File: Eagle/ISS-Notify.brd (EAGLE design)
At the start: 63.5 x 63.5 mm, 68 parts, among them J1 ZX62D-B-5P8, J3 PROTOSPACE2, SW1 9077-1, U1 ATMEGA32U4, U2 MCP7940N, U3 TPS63001, U4 MCP73811, U5 TLC5971, U6 TLC5971, X1 8 MHz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

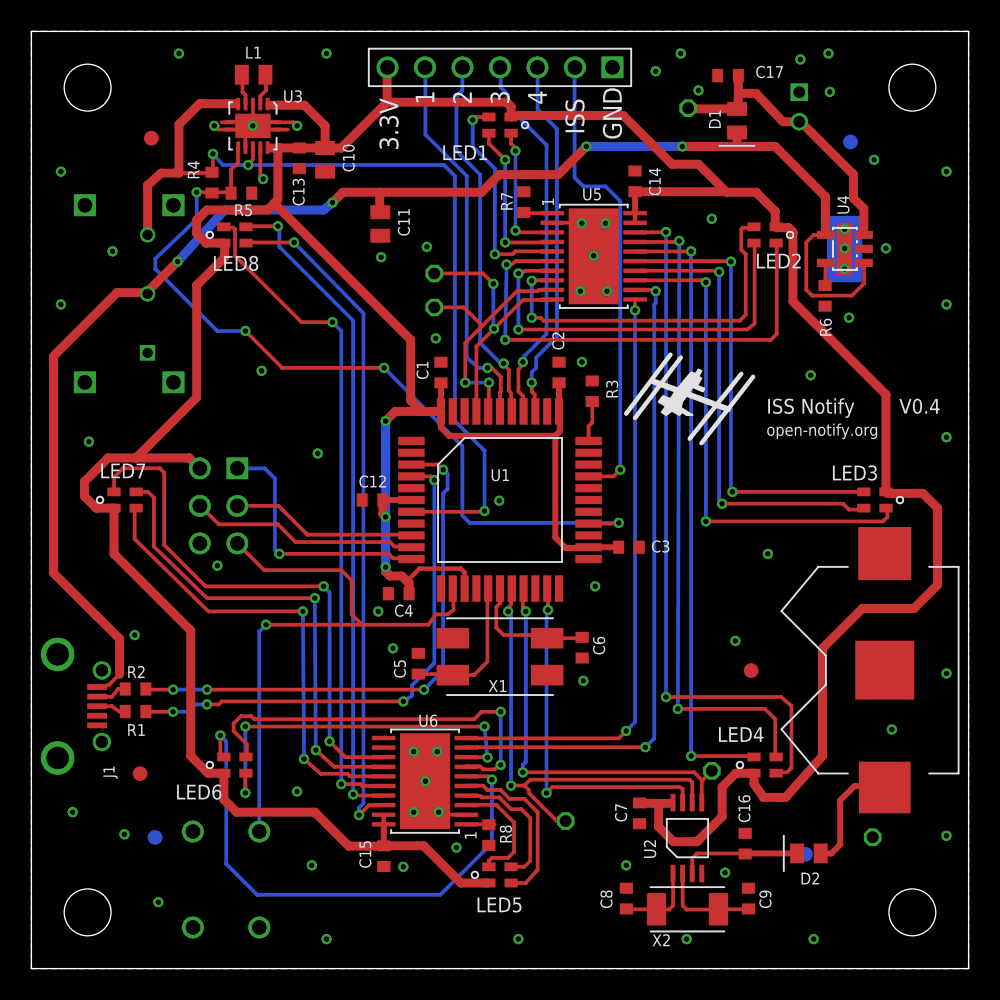
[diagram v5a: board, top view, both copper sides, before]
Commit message: Add fiducials to board and library. Passes DRC, ERC, rats.
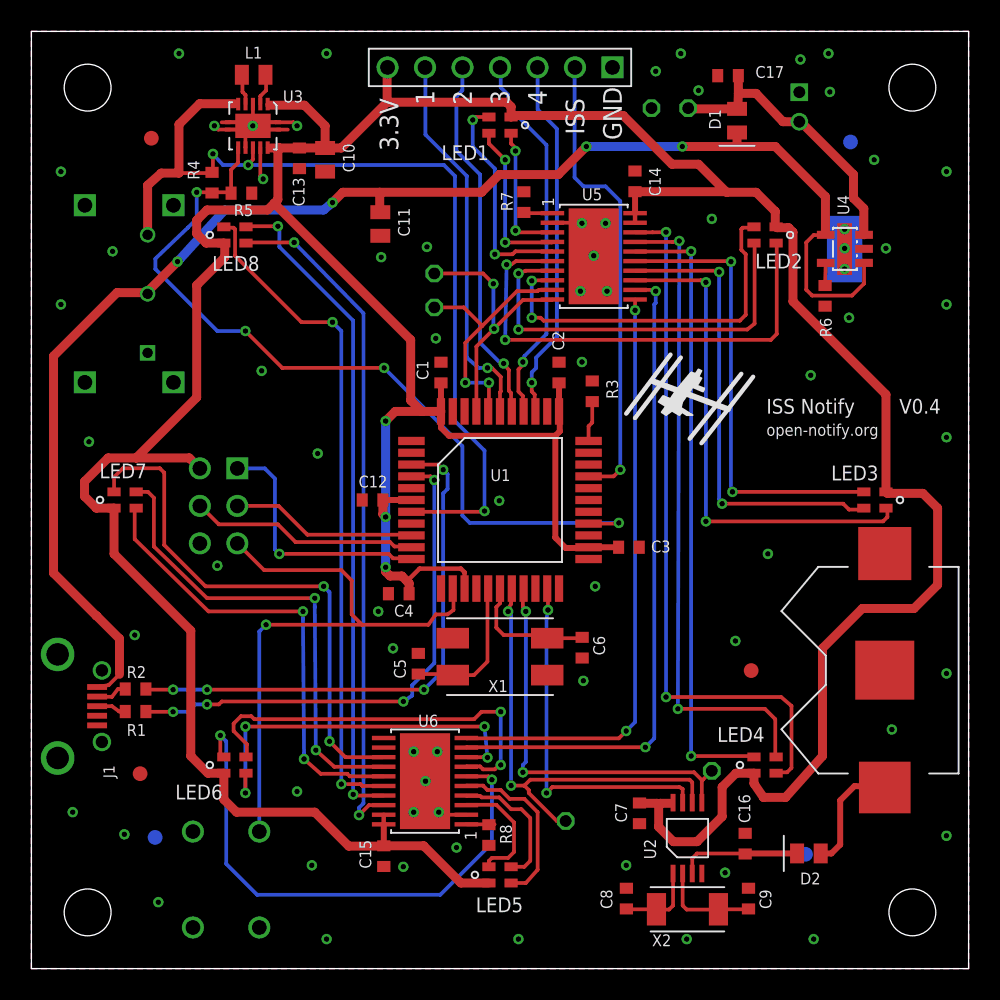
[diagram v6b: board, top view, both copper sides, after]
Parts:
- J1: value ZX62D-B-5P8 -> CON_USB-MICRO-ZX62D-B-5P8; device con-hirose-microusb:ZX62D-B-5P8 -> ISS-Notify:USBMICROSMT-HIROSE
- U$10, U$11, U$6, U$7, U$8, U$9: device adafruit:FIDUCIAL_1MM -> ISS-Notify:FIDUCIAL_1MM
- moved TESTGND 51.6 mm to (42.0, 58.3)
- moved J1 0.25 mm to (1.78, 18.0)
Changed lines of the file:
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@@
 <setting verticaltext="up"/>
 </settings>
-<grid distance="4.75" unitdist="mm" unit="mm" style="dots" multiple="1" display="yes" altdistance="0.025" altunitdist="inch" altunit="inch"/>
+<grid distance="0.005" unitdist="inch" unit="inch" style="dots" multiple="1" display="yes" altdistance="0.025" altunitdist="inch" altunit="inch"/>
 <layers>
 <layer number="1" name="Top" color="4" fill="1" visible="yes" active="yes"/>
@@
 <layer number="14" name="Route14" color="1" fill="6" visible="no" active="yes"/>
 <layer number="15" name="Route15" color="4" fill="6" visible="no" active="yes"/>
-<layer number="16" name="Bottom" color="1" fill="1" visible="yes" active="yes"/>
+<layer number="16" name="Bottom" color="1" fill="1" visible="no" active="yes"/>
 <layer number="17" name="Pads" color="2" fill="1" visible="yes" active="yes"/>
 <layer number="18" name="Vias" color="2" fill="1" visible="yes" active="yes"/>
@@
 <layer number="20" name="Dimension" color="15" fill="1" visible="yes" active="yes"/>
 <layer number="21" name="tPlace" color="7" fill="1" visible="yes" active="yes"/>
-<layer number="22" name="bPlace" color="7" fill="1" visible="yes" active="yes"/>
+<layer number="22" name="bPlace" color="7" fill="1" visible="no" active="yes"/>
 <layer number="23" name="tOrigins" color="15" fill="1" visible="yes" active="yes"/>
-<layer number="24" name="bOrigins" color="15" fill="1" visible="yes" active="yes"/>
+<layer number="24" name="bOrigins" color="15" fill="1" visible="no" active="yes"/>
 <layer number="25" name="tNames" color="7" fill="1" visible="yes" active="yes"/>
-<layer number="26" name="bNames" color="7" fill="1" visible="yes" active="yes"/>
+<layer number="26" name="bNames" color="7" fill="1" visible="no" active="yes"/>
 <layer number="27" name="tValues" color="7" fill="1" visible="no" active="yes"/>
 <layer number="28" name="bValues" color="7" fill="1" visible="no" active="yes"/>
-<layer number="29" name="tStop" color="7" fill="3" visible="no" active="yes"/>
+<layer number="29" name="tStop" color="6" fill="1" visible="no" active="yes"/>
 <layer number="30" name="bStop" color="7" fill="6" visible="no" active="yes"/>
-<layer number="31" name="tCream" color="7" fill="4" visible="no" active="yes"/>
+<layer number="31" name="tCream" color="14" fill="13" visible="no" active="yes"/>
 <layer number="32" name="bCream" color="7" fill="5" visible="no" active="yes"/>
 <layer number="33" name="tFinish" color="6" fill="3" visible="no" active="yes"/>
@@
 <layer number="37" name="tTest" color="7" fill="1" visible="no" active="yes"/>
 <layer number="38" name="bTest" color="7" fill="1" visible="no" active="yes"/>
-<layer number="39" name="tKeepout" color="4" fill="11" visible="yes" active="yes"/>
-<layer number="40" name="bKeepout" color="1" fill="11" visible="yes" active="yes"/>
-<layer number="41" name="tRestrict" color="4" fill="10" visible="yes" active="yes"/>
-<layer number="42" name="bRestrict" color="1" fill="10" visible="yes" active="yes"/>
+<layer number="39" name="tKeepout" color="4" fill="11" visible="no" active="yes"/>
+<layer number="40" name="bKeepout" color="1" fill="11" visible="no" active="yes"/>
+<layer number="41" name="tRestrict" color="4" fill="10" visible="no" active="yes"/>
+<layer number="42" name="bRestrict" color="1" fill="10" visible="no" active="yes"/>
 <layer number="43" name="vRestrict" color="2" fill="10" visible="yes" active="yes"/>
 <layer number="44" name="Drills" color="7" fill="1" visible="no" active="yes"/>
@@
 <layer number="50" name="dxf" color="7" fill="1" visible="no" active="no"/>
 <layer number="51" name="tDocu" color="7" fill="1" visible="yes" active="yes"/>
-<layer number="52" name="bDocu" color="7" fill="1" visible="yes" active="yes"/>
+<layer number="52" name="bDocu" color="7" fill="1" visible="no" active="yes"/>
 <layer number="53" name="tGND_GNDA" color="7" fill="1" visible="no" active="no"/>
 <layer number="54" name="bGND_GNDA" color="7" fill="1" visible="no" active="no"/>
@@
 <layer number="112" name="2Restrict" color="7" fill="1" visible="no" active="yes"/>
 <layer number="113" name="TEMP" color="7" fill="1" visible="yes" active="yes"/>
-<layer number="114" name="TEMP2" color="7" fill="1" visible="yes" active="yes"/>
+<layer number="114" name="TEMP2" color="7" fill="1" visible="no" active="yes"/>
 <layer number="116" name="Patch_BOT" color="7" fill="1" visible="no" active="yes"/>
 <layer number="121" name="_tsilk" color="7" fill="1" visible="no" active="yes"/>
@@
 <element name="TESTDATA" library="ISS-Notify" package="TESTPIN" value="TESTPIN" x="27.3" y="44.8"/>
 <element name="TESTCLOCK" library="ISS-Notify" package="TESTPIN" value="TESTPIN" x="27.3" y="47.1"/>
-<element name="TESTGND" library="ISS-Notify" package="TESTPIN" value="TESTPIN" x="57" y="8.9"/>
-<element name="J1" library="con-hirose-microusb" package="ZX62D-B-5P8" value="ZX62D-B-5P8" x="1.778" y="17.78" rot="R270"/>
-<element name="U$6" library="adafruit" package="FIDUCIAL_1MM" value="FIDUCIAL" x="8.128" y="56.261"/>
-<element name="U$7" library="adafruit" package="FIDUCIAL_1MM" value="FIDUCIAL" x="8.382" y="8.89" rot="MR0"/>
-<element name="U$8" library="adafruit" package="FIDUCIAL_1MM" value="FIDUCIAL" x="7.366" y="13.208"/>
-<element name="U$9" library="adafruit" package="FIDUCIAL_1MM" value="FIDUCIAL" x="48.768" y="20.193"/>
-<element name="U$10" library="adafruit" package="FIDUCIAL_1MM" value="FIDUCIAL" x="55.499" y="56.007" rot="MR0"/>
-<element name="U$11" library="adafruit" package="FIDUCIAL_1MM" value="FIDUCIAL" x="52.451" y="7.747" rot="MR0"/>
+<element name="TESTGND" library="ISS-Notify" package="TESTPIN" value="TESTPIN" x="42.014" y="58.303"/>
+<element name="J1" library="ISS-Notify" package="USBMICROSMT-HIROSE" value="CON_USB-MICRO-ZX62D-B-5P8" x="1.778" y="18.034" rot="R270"/>
+<element name="U$6" library="ISS-Notify" package="FIDUCIAL_1MM" value="FIDUCIAL" x="8.128" y="56.261"/>
+<element name="U$7" library="ISS-Notify" package="FIDUCIAL_1MM" value="FIDUCIAL" x="8.382" y="8.89" rot="MR0"/>
+<element name="U$8" library="ISS-Notify" package="FIDUCIAL_1MM" value="FIDUCIAL" x="7.366" y="13.208"/>
+<element name="U$9" library="ISS-Notify" package="FIDUCIAL_1MM" value="FIDUCIAL" x="48.768" y="20.193"/>
+<element name="U$10" library="ISS-Notify" package="FIDUCIAL_1MM" value="FIDUCIAL" x="55.499" y="56.007" rot="MR0"/>
+<element name="U$11" library="ISS-Notify" package="FIDUCIAL_1MM" value="FIDUCIAL" x="52.451" y="7.747" rot="MR0"/>
 </elements>
 <signals>
@@
 </signal>
 </signals>
-<errors>
-</errors>
 </board>
 </drawing>

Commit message: Changed resistor values for the LED according to datasheet
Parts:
- R7, R8: value 1 k -> 10 k
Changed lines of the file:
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@@
 <?xml version="1.0" encoding="utf-8"?>
 <!DOCTYPE eagle SYSTEM "eagle.dtd">
-<eagle version="6.4">
+<eagle version="7.1.0">
 <drawing>
 <settings>
@@
 <pass name="Default">
 <param name="RoutingGrid" value="50mil"/>
+<param name="AutoGrid" value="1"/>
+<param name="Efforts" value="0"/>
+<param name="TopRouterVariant" value="1"/>
 <param name="tpViaShape" value="round"/>
 <param name="PrefDir.1" value="|"/>
@@
 <attribute name="NAME" x="27.57" y="17.2" size="0.8128" layer="21" font="vector" ratio="20" rot="R180"/>
 </element>
-<element name="R7" library="rcl_custom" package="0603-C-NOSILK" value="1 k" x="33.362" y="51.934" smashed="yes" rot="R270">
+<element name="R7" library="rcl_custom" package="0603-C-NOSILK" value="10 k" x="33.362" y="51.934" smashed="yes" rot="R270">
 <attribute name="NAME" x="31.812" y="52.634" size="0.8" layer="25" font="vector" ratio="20" rot="R270"/>
 <attribute name="VALUE" x="31.362" y="52.734" size="1" layer="27" ratio="10" rot="R270"/>
 </element>
-<element name="R8" library="rcl_custom" package="0603-C-NOSILK" value="1 k" x="30.998" y="9.05" smashed="yes" rot="R90">
+<element name="R8" library="rcl_custom" package="0603-C-NOSILK" value="10 k" x="30.998" y="9.05" smashed="yes" rot="R90">
 <attribute name="NAME" x="32.548" y="8.45" size="0.8" layer="25" font="vector" ratio="20" rot="R90"/>
 <attribute name="VALUE" x="32.998" y="8.25" size="1" layer="27" ratio="10" rot="R90"/>
